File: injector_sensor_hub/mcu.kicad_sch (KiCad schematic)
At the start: 17 parts, among them J2 Programming Header, U1 MCP2562, U2 PIC18F26K83, Y1 Crystal

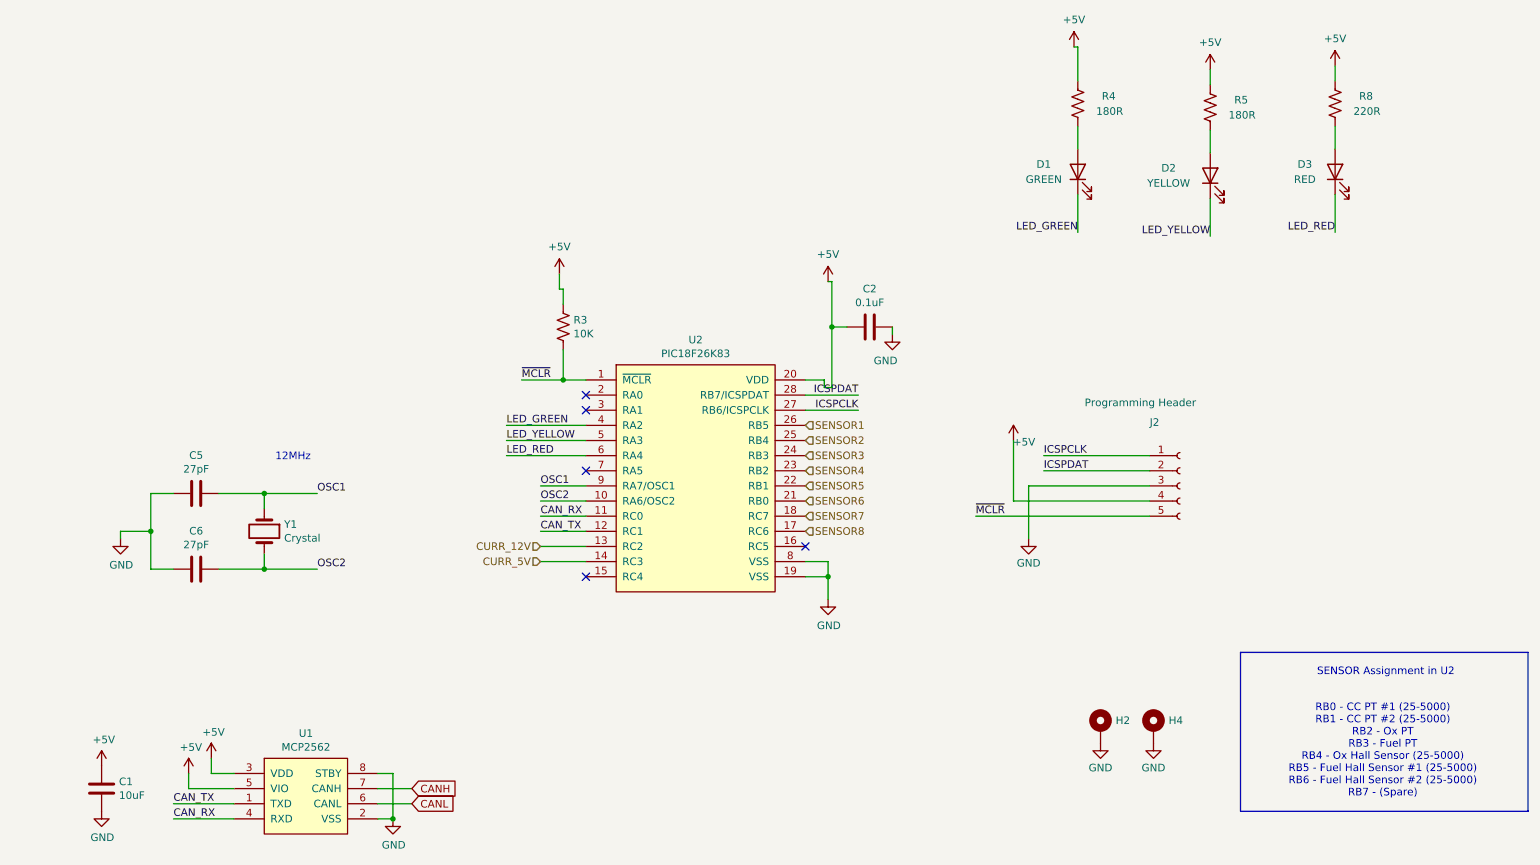
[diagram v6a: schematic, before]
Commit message: revert changes to daq and propulsion board
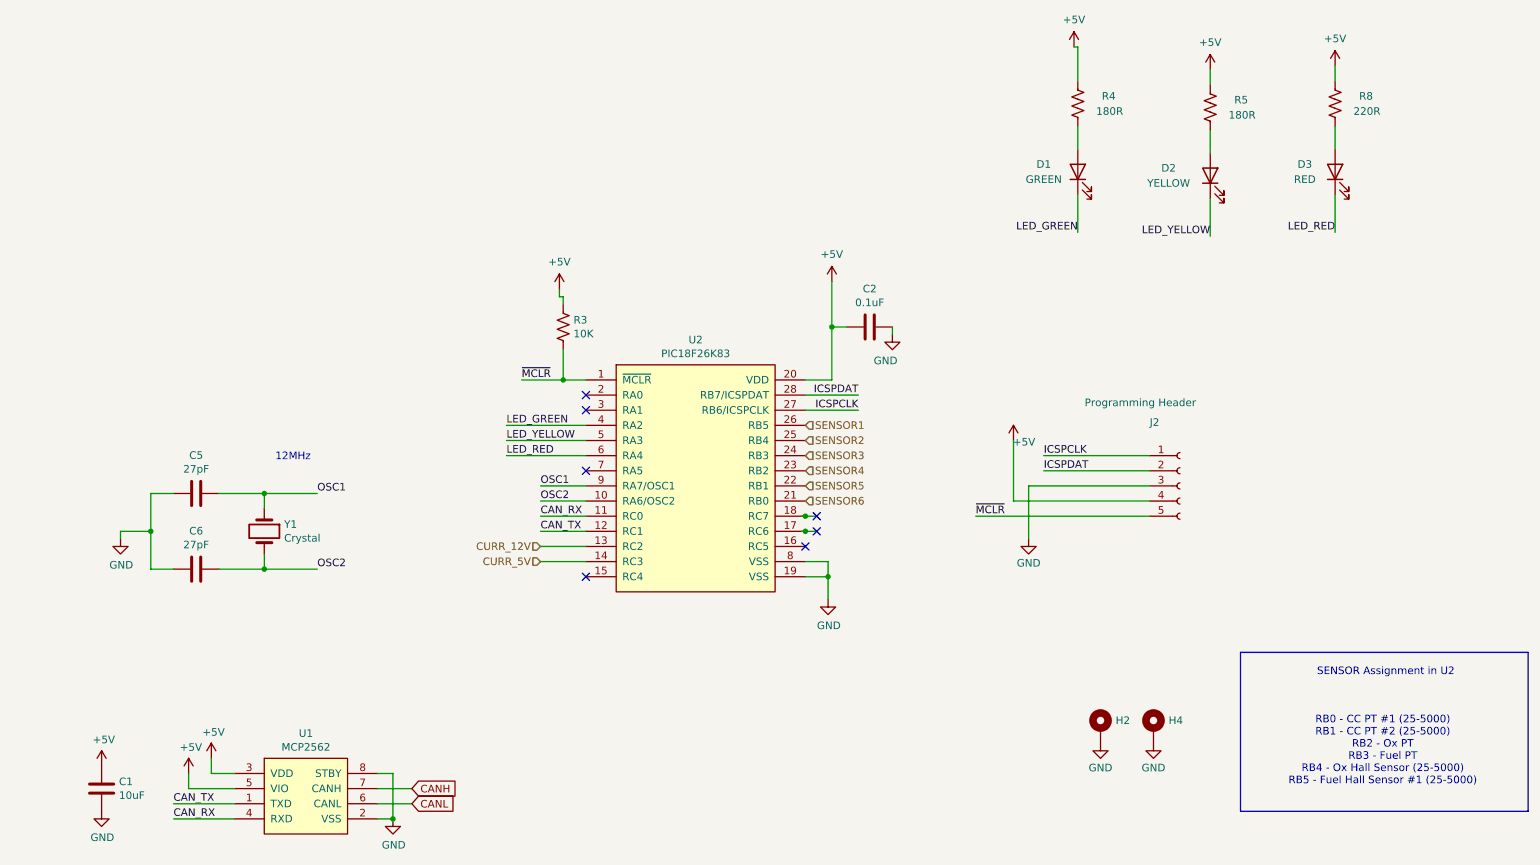
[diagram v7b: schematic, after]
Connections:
- net SENSOR7: no longer names the net of U2.18 (RC7)
- net SENSOR8: no longer names the net of U2.17 (RC6)
- no-connect marks 5 -> 7
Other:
- note added: "RB0 - CC PT #1 (25-5000) RB1 - CC PT #2 (25-5000) RB2 - Ox PT RB3 - Fuel PT RB4 - Ox Hall Sensor (25-5000) RB5 - Fuel Hall Sensor #1 (25-5000)"
- note removed: "RB0 - CC PT #1 (25-5000) RB1 - CC PT #2 (25-5000) RB2 - Ox PT RB3 - Fuel PT RB4 - Ox Hall Sensor (25-5000) RB5 - Fuel Hall Sensor #1 (25-5000) RB6 - Fuel Hall Sensor #2 (25-5000) RB7 - (Spare)"
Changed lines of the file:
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@@
 	(paper "A4")
 	(junction
+		(at 159.385 111.76)
+		(diameter 0)
+		(color 0 0 0 0)
+	)
+	(junction
 		(at 118.745 88.9)
 		(diameter 0)
@@
 		(color 0 0 0 0)
 	)
+	(junction
+		(at 159.385 114.3)
+		(diameter 0)
+		(color 0 0 0 0)
+	)
 	(no_connect
 		(at 122.555 104.14)
@@
 	)
 	(no_connect
+		(at 161.29 111.76)
+	)
+	(no_connect
+		(at 161.29 114.3)
+	)
+	(no_connect
 		(at 122.555 93.98)
 	)
@@
 	(wire
 		(pts
-			(xy 163.83 80.01) (xy 163.83 90.17)
+			(xy 163.83 80.01) (xy 163.83 88.9)
 		)
 		(stroke
@@
 	(wire
 		(pts
-			(xy 49.53 120.65) (xy 53.34 120.65)
+			(xy 158.75 114.3) (xy 159.385 114.3)
 		)
 		(stroke
@@
 	(wire
 		(pts
-			(xy 162.56 88.9) (xy 159.385 88.9)
+			(xy 49.53 120.65) (xy 53.34 120.65)
 		)
 		(stroke
@@
 	(wire
 		(pts
-			(xy 60.96 107.95) (xy 68.58 107.95)
+			(xy 163.83 88.9) (xy 159.385 88.9)
 		)
 		(stroke
@@
 	(wire
 		(pts
-			(xy 162.56 90.17) (xy 163.83 90.17)
+			(xy 60.96 107.95) (xy 68.58 107.95)
 		)
 		(stroke
@@
 	(wire
 		(pts
-			(xy 118.11 73.66) (xy 118.745 73.66)
+			(xy 59.69 154.94) (xy 63.5 154.94)
 		)
 		(stroke
@@
 	(wire
 		(pts
-			(xy 59.69 154.94) (xy 63.5 154.94)
+			(xy 68.58 120.65) (xy 68.58 118.11)
 		)
 		(stroke
@@
 	(wire
 		(pts
-			(xy 68.58 120.65) (xy 68.58 118.11)
+			(xy 159.385 114.3) (xy 161.29 114.3)
 		)
 		(stroke
@@
 	(wire
 		(pts
-			(xy 163.83 72.39) (xy 163.195 72.39)
-		)
-		(stroke
-			(width 0)
-			(type default)
-		)
-	)
-	(wire
-		(pts
 			(xy 90.17 154.94) (xy 90.17 162.56)
 		)
@@
 	(wire
 		(pts
-			(xy 118.11 71.12) (xy 118.11 73.66)
+			(xy 159.385 111.76) (xy 161.29 111.76)
 		)
 		(stroke
@@
 	(wire
 		(pts
+			(xy 118.11 74.93) (xy 118.745 74.93)
+		)
+		(stroke
+			(width 0)
+			(type default)
+		)
+	)
+	(wire
+		(pts
 			(xy 53.34 107.95) (xy 49.53 107.95)
 		)
@@
 	(wire
 		(pts
-			(xy 162.56 90.17) (xy 162.56 88.9)
+			(xy 158.75 111.76) (xy 159.385 111.76)
 		)
 		(stroke
@@
 	(wire
 		(pts
-			(xy 118.745 73.66) (xy 118.745 76.2)
+			(xy 118.11 73.66) (xy 118.11 74.93)
 		)
 		(stroke
@@
 	(wire
 		(pts
+			(xy 118.745 74.93) (xy 118.745 76.2)
+		)
+		(stroke
+			(width 0)
+			(type default)
+		)
+	)
+	(wire
+		(pts
 			(xy 159.385 119.38) (xy 163.195 119.38)
 		)
@@
 		)
 	)
-	(text "RB0 - CC PT #1 (25-5000)\nRB1 - CC PT #2 (25-5000)\nRB2 - Ox PT\nRB3 - Fuel PT\nRB4 - Ox Hall Sensor (25-5000)\nRB5 - Fuel Hall Sensor #1 (25-5000)\nRB6 - Fuel Hall Sensor #2 (25-5000)\nRB7 - (Spare)\n\n"
+	(text "RB0 - CC PT #1 (25-5000)\nRB1 - CC PT #2 (25-5000)\nRB2 - Ox PT\nRB3 - Fuel PT\nRB4 - Ox Hall Sensor (25-5000)\nRB5 - Fuel Hall Sensor #1 (25-5000)\n\n"
 		(exclude_from_sim no)
 		(at 256.286 152.146 0)
@@
 		)
 	)
-	(hierarchical_label "SENSOR8"
-		(shape input)
-		(at 159.385 114.3 0)
-		(fields_autoplaced yes)
-		(effects
-			(font
-				(size 1.27 1.27)
-			)
-			(justify left)
-		)
-	)
 	(hierarchical_label "SENSOR2"
 		(shape input)
@@
 		)
 	)
-	(hierarchical_label "SENSOR7"
-		(shape input)
-		(at 159.385 111.76 0)
-		(fields_autoplaced yes)
-		(effects
-			(font
-				(size 1.27 1.27)
-			)
-			(justify left)
-		)
-	)
 	(hierarchical_label "SENSOR5"
 		(shape input)
@@
 		(lib_name "+3V3_1")
 		(lib_id "power:+3V3")
-		(at 163.195 72.39 0)
+		(at 163.83 72.39 0)
 		(unit 1)
 		(exclude_from_sim no)
@@
 		(dnp no)
 		(property "Reference" "#PWR08"
-			(at 163.195 76.2 0)
+			(at 163.83 76.2 0)
 			(effects
 				(font
@@
 		)
 		(property "Value" "+5V"
-			(at 163.195 67.818 0)
+			(at 163.83 67.818 0)
 			(effects
 				(font
@@
 		)
 		(property "Footprint" ""
-			(at 163.195 72.39 0)
+			(at 163.83 72.39 0)
 			(effects
 				(font
@@
 		)
 		(property "Datasheet" ""
-			(at 163.195 72.39 0)
+			(at 163.83 72.39 0)
 			(effects
 				(font
@@
 		)
 		(property "Description" ""
-			(at 163.195 72.39 0)
+			(at 163.83 72.39 0)
 			(effects
 				(font
@@
 		(lib_name "+3V3_1")
 		(lib_id "power:+3V3")
-		(at 118.11 71.12 0)
+		(at 118.11 73.66 0)
 		(unit 1)
 		(exclude_from_sim no)
@@
 		(dnp no)
 		(property "Reference" "#PWR013"
-			(at 118.11 74.93 0)
+			(at 118.11 77.47 0)
 			(effects
 				(font
@@
 		)
 		(property "Value" "+5V"
-			(at 118.11 66.548 0)
+			(at 118.11 69.088 0)
 			(effects
 				(font
@@
 		)
 		(property "Footprint" ""
-			(at 118.11 71.12 0)
+			(at 118.11 73.66 0)
 			(effects
 				(font
@@
 		)
 		(property "Datasheet" ""
-			(at 118.11 71.12 0)
+			(at 118.11 73.66 0)
 			(effects
 				(font
@@
 		)
 		(property "Description" ""
-			(at 118.11 71.12 0)
+			(at 118.11 73.66 0)
 			(effects
 				(font

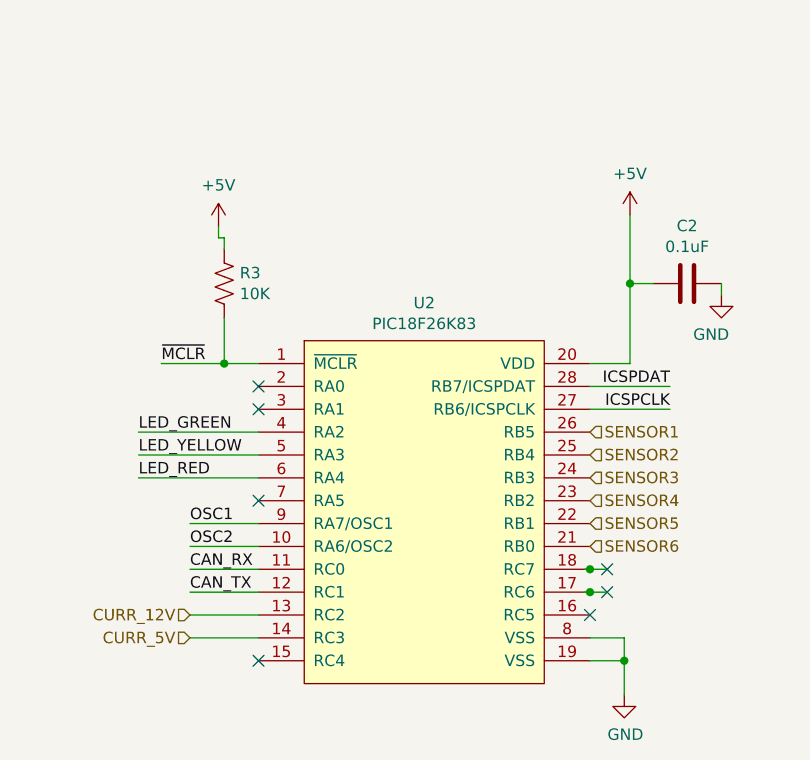
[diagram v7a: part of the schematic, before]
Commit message: fixed J1 connector to right pins and cleaned up schematic wiring
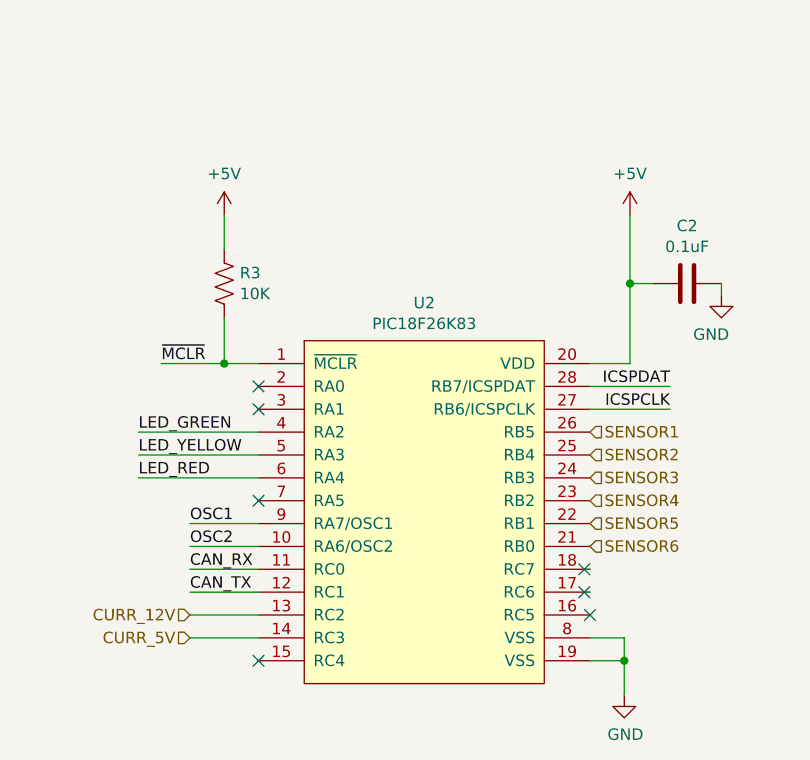
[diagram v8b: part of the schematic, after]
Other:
- title: (none) -> Injector Sensor Hub 
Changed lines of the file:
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@@
 	(generator_version "8.0")
 	(paper "A4")
-	(junction
-		(at 159.385 111.76)
-		(diameter 0)
-		(color 0 0 0 0)
+	(title_block
+		(title "Injector Sensor Hub ")
 	)
 	(junction
@@
 		(color 0 0 0 0)
 	)
-	(junction
-		(at 159.385 114.3)
-		(diameter 0)
-		(color 0 0 0 0)
-	)
 	(no_connect
 		(at 122.555 104.14)
@@
 	)
 	(no_connect
-		(at 161.29 111.76)
+		(at 158.75 111.76)
 	)
 	(no_connect
-		(at 161.29 114.3)
+		(at 158.75 114.3)
 	)
 	(no_connect
@@
 	(wire
 		(pts
-			(xy 159.385 114.3) (xy 161.29 114.3)
-		)
-		(stroke
-			(width 0)
-			(type default)
-		)
-	)
-	(wire
-		(pts
 			(xy 173.99 80.01) (xy 173.99 81.28)
 		)
@@
 	(wire
 		(pts
-			(xy 159.385 111.76) (xy 161.29 111.76)
-		)
-		(stroke
-			(width 0)
-			(type default)
-		)
-	)
-	(wire
-		(pts
 			(xy 109.22 96.52) (xy 122.555 96.52)
 		)
@@
 	(wire
 		(pts
-			(xy 118.11 74.93) (xy 118.745 74.93)
-		)
-		(stroke
-			(width 0)
-			(type default)
-		)
-	)
-	(wire
-		(pts
 			(xy 53.34 107.95) (xy 49.53 107.95)
 		)
@@
 	(wire
 		(pts
-			(xy 118.11 73.66) (xy 118.11 74.93)
+			(xy 118.745 72.39) (xy 118.745 76.2)
 		)
 		(stroke
@@
 	(wire
 		(pts
-			(xy 118.745 74.93) (xy 118.745 76.2)
-		)
-		(stroke
-			(width 0)
-			(type default)
-		)
-	)
-	(wire
-		(pts
 			(xy 159.385 119.38) (xy 163.195 119.38)
 		)
@@
 		(lib_name "+3V3_1")
 		(lib_id "power:+3V3")
-		(at 118.11 73.66 0)
+		(at 118.745 72.39 0)
 		(unit 1)
 		(exclude_from_sim no)
@@
 		(dnp no)
 		(property "Reference" "#PWR013"
-			(at 118.11 77.47 0)
+			(at 118.745 76.2 0)
 			(effects
 				(font
@@
 		)
 		(property "Value" "+5V"
-			(at 118.11 69.088 0)
+			(at 118.745 67.818 0)
 			(effects
 				(font
@@
 		)
 		(property "Footprint" ""
-			(at 118.11 73.66 0)
+			(at 118.745 72.39 0)
 			(effects
 				(font
@@
 		)
 		(property "Datasheet" ""
-			(at 118.11 73.66 0)
+			(at 118.745 72.39 0)
 			(effects
 				(font
@@
 		)
 		(property "Description" ""
-			(at 118.11 73.66 0)
+			(at 118.745 72.39 0)
 			(effects
 				(font
